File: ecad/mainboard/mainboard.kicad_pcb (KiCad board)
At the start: 4 copper layers, 340 x 220 mm, 124 parts, among them J1 TYPE-C-31-M-12, J2 SWD, J3 UART, SW1 TS-1187A-B-A-B, SW2 TS-1187A-B-A-B, SW3 SW_Push, SW4 SW_Push, U1 NCP1117ST33T3G, U10 DRV5056A3xQDBZxR, U11 DRV5056A3xQDBZxR, U12 DRV5056A3xQDBZxR, U13 DRV5056A3xQDBZxR, U14 DRV5056A3xQDBZxR, U15 DRV5056A3xQDBZxR, U16 DRV5056A3xQDBZxR, U17 DRV5056A3xQDBZxR, U18 DRV5056A3xQDBZxR, U19 DRV5056A3xQDBZxR, U2 USBLC6-2SC6, U20 DRV5056A3xQDBZxR, U21 DRV5056A3xQDBZxR, U22 CD4051BM96, U23 CD4051BM96, U3 W25Q128JVS, U4 74AHCT1G125, U5 RP2040, U6 DRV5056A3xQDBZxR, U7 DRV5056A3xQDBZxR, U8 DRV5056A3xQDBZxR, U9 DRV5056A3xQDBZxR, Y1 ABM8-272-T3

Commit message: WIP: PCB case
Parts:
- C13, C14: value 1u -> 1uF
- D2, D3: value SK6812MINI -> SK6812MINI-EA
- J1: footprint Connector_USB:USB_C_Receptacle_HRO_TYPE-C-31-M-12 -> Udong:USB_C_Receptacle_HRO_TYPE-C-31-M-12
- J2: footprint Connector_JST:JST_SH_BM03B-SRSS-TB_1x03-1MP_P1.00mm_Vertical -> Udong:JST_SH_BM03B-SRSS-TB_1x03-1MP_P1.00mm_Vertical
- moved C32 20.0 mm to (173.5, 136.8)
- moved C36 20.0 mm to (143.6, 131.5)
- moved C37 20.0 mm to (335.6, 147.6)
- moved C38 20.0 mm to (333.4, 136.8)
- moved C11 20.0 mm to (218.7, 65.7)
- moved C18 20.0 mm to (207.0, 77.9)
- moved C19 20.0 mm to (210.2, 77.9)
- moved R13 20.0 mm to (208.7, 76.0)
- moved SW4 20.0 mm to (362.3, 67.2)
- moved R5 20.0 mm to (194.6, 51.6)
- moved C10 20.0 mm to (216.6, 71.9)
- moved C13 20.0 mm to (213.2, 64.0)
- moved C14 20.0 mm to (214.2, 64.0)
- moved C15 20.0 mm to (206.1, 56.6)
- moved C16 20.0 mm to (338.8, 60.5)
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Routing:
- net +1V1: track 15.5 -> 11.8 mm
- net GND: track 153.4 -> 151.8 mm, vias 50 -> 52
- net USB_D+: track 8.52 -> 9.72 mm
- net USB_D-: track 8.57 -> 9.76 mm
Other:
- board text added: "GND"
- board text added: "RX"
- board text added: "SWCLK"
- board text added: "SWD"
- board text added: "TX"

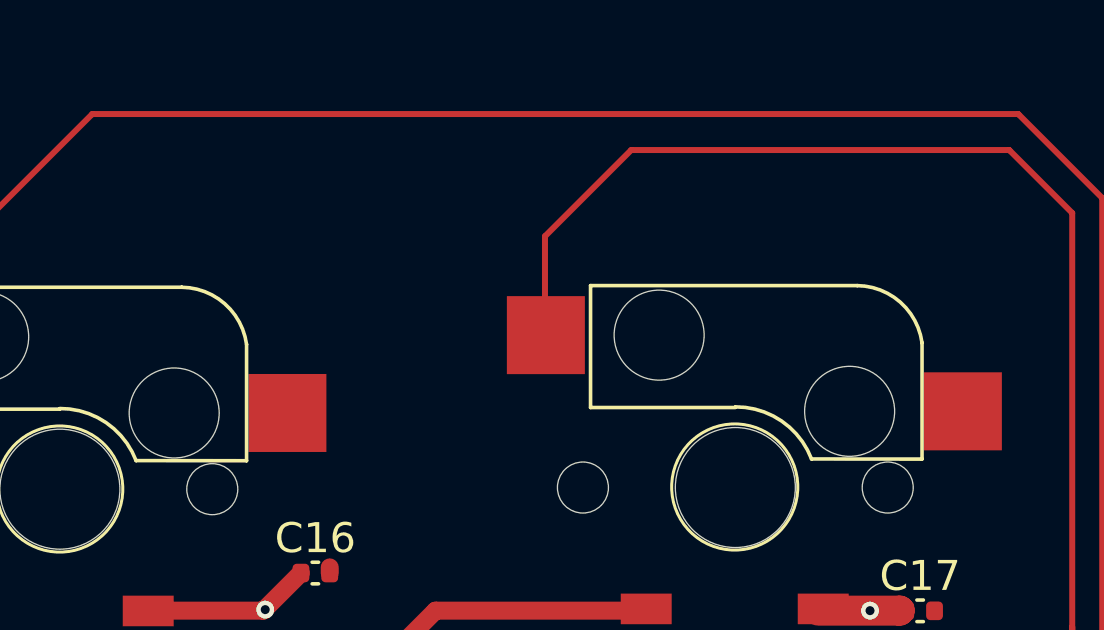
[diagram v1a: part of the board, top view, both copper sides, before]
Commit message: Put labels about button assignment on User.comments layer
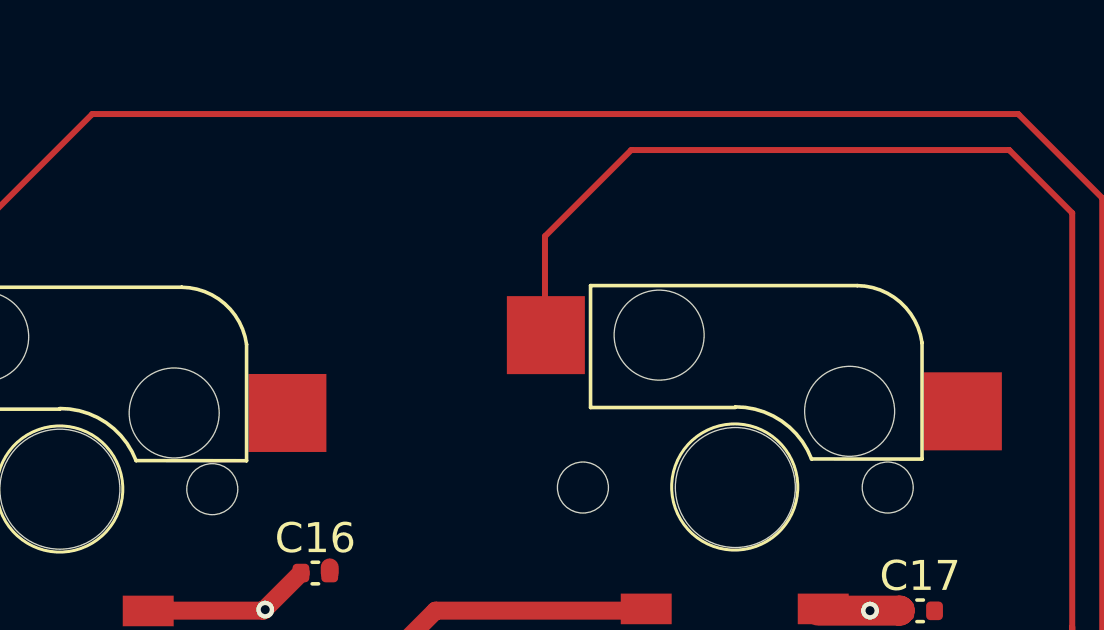
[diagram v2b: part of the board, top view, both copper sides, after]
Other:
- board text added: "M0_0"
- board text added: "M0_1"
- board text added: "M0_2"
- board text added: "M0_3"
- board text added: "M0_4"
- board text added: "M0_5"
- board text added: "M0_6"
- board text added: "M0_7"
- board text added: "M1_10"
- board text added: "M1_11"
- board text added: "M1_12"
- board text added: "M1_13"
- board text added: "M1_14"
- board text added: "M1_15"
- board text added: "M1_8"
- board text added: "M1_9"
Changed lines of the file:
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@@
 		(fp_arc
 			(start 5.436 16.231)
-			(mid 4.002296 15.679932)
+			(mid 4.002293 15.679933)
 			(end 3.277 14.326)
 			(stroke
@@
 		(fp_arc
 			(start 5.436 16.231)
-			(mid 4.002296 15.679932)
+			(mid 4.002293 15.679933)
 			(end 3.277 14.326)
 			(stroke
@@
 		)
 	)
+	(gr_text "M0_4"
+		(at 89 136 0)
+		(layer "Cmts.User")
+		(effects
+			(font
+				(size 3 3)
+				(thickness 0.2)
+			)
+			(justify left bottom)
+		)
+	)
+	(gr_text "M0_5"
+		(at 185 138 0)
+		(layer "Cmts.User")
+		(effects
+			(font
+				(size 3 3)
+				(thickness 0.2)
+			)
+			(justify left bottom)
+		)
+	)
+	(gr_text "M1_9\n"
+		(at 196 158 0)
+		(layer "Cmts.User")
+		(effects
+			(font
+				(size 3 3)
+				(thickness 0.2)
+			)
+			(justify left bottom)
+		)
+	)
+	(gr_text "M0_2"
+		(at 76 102 0)
+		(layer "Cmts.User")
+		(effects
+			(font
+				(size 3 3)
+				(thickness 0.2)
+			)
+			(justify left bottom)
+		)
+	)
+	(gr_text "M0_7"
+		(at 153 131 0)
+		(layer "Cmts.User")
+		(effects
+			(font
+				(size 3 3)
+				(thickness 0.2)
+			)
+			(justify left bottom)
+		)
+	)
+	(gr_text "M1_8"
+		(at 338 130 0)
+		(layer "Cmts.User")
+		(effects
+			(font
+				(size 3 3)
+				(thickness 0.2)
+			)
+			(justify left bottom)
+		)
+	)
+	(gr_text "M1_13\n"
+		(at 312 110 0)
+		(layer "Cmts.User")
+		(effects
+			(font
+				(size 3 3)
+				(thickness 0.2)
+			)
+			(justify left bottom)
+		)
+	)
+	(gr_text "M1_14"
+		(at 257 131 0)
+		(layer "Cmts.User")
+		(effects
+			(font
+				(size 3 3)
+				(thickness 0.2)
+			)
+			(justify left bottom mirror)
+		)
+	)
+	(gr_text "M0_1"
+		(at 116 100 0)
+		(layer "Cmts.User")
+		(effects
+			(font
+				(size 3 3)
+				(thickness 0.2)
+			)
+			(justify left bottom)
+		)
+	)
+	(gr_text "M1_12\n"
+		(at 224 166 0)
+		(layer "Cmts.User")
+		(effects
+			(font
+				(size 3 3)
+				(thickness 0.2)
+			)
+			(justify left bottom)
+		)
+	)
+	(gr_text "M1_15\n"
+		(at 285 98 0)
+		(layer "Cmts.User")
+		(effects
+			(font
+				(size 3 3)
+				(thickness 0.2)
+			)
+			(justify left bottom)
+		)
+	)
+	(gr_text "M0_0"
+		(at 148 95 0)
+		(layer "Cmts.User")
+		(effects
+			(font
+				(size 3 3)
+				(thickness 0.2)
+			)
+			(justify left bottom)
+		)
+	)
+	(gr_text "M1_10"
+		(at 207 111 0)
+		(layer "Cmts.User")
+		(effects
+			(font
+				(size 3 3)
+				(thickness 0.2)
+			)
+			(justify left bottom)
+		)
+	)
+	(gr_text "M1_11\n"
+		(at 292 77 0)
+		(layer "Cmts.User")
+		(effects
+			(font
+				(size 3 3)
+				(thickness 0.2)
+			)
+			(justify left bottom)
+		)
+	)
+	(gr_text "M0_3\n"
+		(at 180 100 0)
+		(layer "Cmts.User")
+		(effects
+			(font
+				(size 3 3)
+				(thickness 0.2)
+			)
+			(justify left bottom)
+		)
+	)
+	(gr_text "M0_6"
+		(at 116 131 0)
+		(layer "Cmts.User")
+		(effects
+			(font
+				(size 3 3)
+				(thickness 0.2)
+			)
+			(justify left bottom)
+		)
+	)

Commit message: Update circuit for the new design
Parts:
- J2: footprint Udong:JST_SH_BM03B-SRSS-TB_1x03-1MP_P1.00mm_Vertical -> Connector_JST:JST_SH_SM03B-SRSS-TB_1x03-1MP_P1.00mm_Horizontal
- moved J2 0.16 mm to (153.6, 43.6), turned to 180 degrees
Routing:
- net SWCLK: track 87.5 -> 88.3 mm
- net SWD: track 92.7 -> 92.1 mm, vias 2 -> 0
- net GND: vias 52 -> 50

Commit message: Update PCB. Next task would be move switch positions
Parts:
- removed C16, C17: 1uF, Capacitor_SMD:C_0402_1005Metric
- removed D2, D3: SK6812MINI-EA, Udong:MX_Socket_LED
- removed J3: UART, Connector_PinSocket_2.54mm:PinSocket_1x03_P2.54mm_Horizontal
- removed R12: 560, Resistor_SMD:R_0402_1005Metric
- removed R4, R6: 20k, Resistor_SMD:R_0402_1005Metric
- removed SW1, SW2: TS-1187A-B-A-B, Button_Switch_SMD:SW_Push_1P1T_XKB_TS-1187A
- removed U4: 74AHCT1G125, Package_TO_SOT_SMD:SOT-353_SC-70-5
- added R30: 10k, Resistor_SMD:R_0402_1005Metric, F.Cu at (203.7, 71.0)
- added R32: 1k, Resistor_SMD:R_0402_1005Metric, F.Cu at (204.1, 69.2)
- added R9: 10k, Resistor_SMD:R_0402_1005Metric, F.Cu at (197.7, 56.7)
- R1: value 220k -> 10k
- R10, R11: footprint Resistor_SMD:R_0402_1005Metric -> Resistor_SMD:R_0603_1608Metric
- moved SW4 267.5 mm to (94.7, 66.2)
- moved SW3 217.4 mm to (122.4, 66.5)
- moved H10 69.5 mm to (175.0, 190.0)
- moved H2 63.2 mm to (70.0, 190.0)
- moved H3 63.2 mm to (350.0, 190.0)
- moved C20 50.0 mm to (85.8, 79.6)
- moved H7 31.6 mm to (255.0, 190.0)
- moved H6 28.5 mm to (256.5, 49.5)
- moved H1 20.0 mm to (70.0, 50.0)
- moved H4 20.0 mm to (350.0, 50.0)
- moved J2 15.5 mm to (169.0, 43.3)
- moved R8 15.0 mm to (221.9, 44.4), turned to 0 degrees
- moved R1 13.5 mm to (217.8, 70.8), turned to 0 degrees
- moved D1 13.5 mm to (219.1, 44.4), turned to 0 degrees
- moved H5 11.3 mm to (146.3, 50.1)
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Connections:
- R1 pad 1: +3.3V -> Net-(U5-GPIO23)
- R1 pad 2: REF_0.6V -> GND
- R5 pad 2: Net-(R5-Pad2) -> BOOTSEL_SW
- SW4 pad 1: DS_1_IN -> BOOTSEL_SW
- U5 pad 2: UART_TX -> GND
- U5 pad 26: RUN -> unconnected-(U5-RUN-Pad26)
- U5 pad 3: UART_RX -> GND
- U5 pad 34: DS_0_IN -> GND
- U5 pad 35: DS_1_IN -> Net-(U5-GPIO23)
- U5 pad 36: LED_OUT -> GND
- U5 pad 4: GND -> DS_0_IN
- U5 pad 5: GND -> DS_1_IN
- U5 pad 6: REF_0.6V -> GND
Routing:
- net BOOTSEL_SW: track 0.00 -> 163.1 mm, vias 0 -> 2
- net LED_OUT_5V: track 94.8 -> 0.00 mm
- net DS_0_IN: track 215.1 -> 126.0 mm, vias 0 -> 2
- net DS_1_IN: track 83.5 -> 2.09 mm
- net RUN: track 58.5 -> 0.00 mm, vias 2 -> 0
- net UART_RX: track 53.0 -> 0.00 mm
- net UART_TX: track 48.1 -> 0.00 mm
- net LED_OUT: track 29.8 -> 0.00 mm
- net GPIO25: track 13.5 -> 34.6 mm
- net Net-(D2-DOUT): track 17.6 -> 0.00 mm
- net GND: track 151.8 -> 135.1 mm, vias 50 -> 42
- net VBUS: track 35.2 -> 22.9 mm, vias 5 -> 2
- net Net-(R5-Pad2): track 11.2 -> 0.00 mm
- net SWD: track 92.1 -> 85.1 mm
- net SWCLK: track 88.3 -> 81.7 mm
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- removed copper zone on In2.Cu, net VBUS
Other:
- board size 340 x 220 mm -> 301.3 x 160 mm
- board text added: "Debug"
- board text removed: "RX"
- board text removed: "TX"

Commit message: Now, Webconf is the root source of switchs coordinates
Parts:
- moved U16 0.10 mm to (205.1, 120.0)
- moved U15 0.08 mm to (190.0, 167.5)
- moved U20 0.08 mm to (250.0, 117.5)
- moved U10 0.08 mm to (85.0, 147.5)
- moved U14 0.08 mm to (335.0, 142.5)
- moved U19 0.08 mm to (310.0, 117.5)
- moved U21 0.08 mm to (280.0, 107.5)
- moved U11 0.06 mm to (175.0, 142.5)
- moved U6 0.06 mm to (145.0, 105.0)
- moved U7 0.06 mm to (115.0, 110.0)
- moved U8 0.06 mm to (85.0, 115.0)
- moved U9 0.06 mm to (175.0, 110.0)
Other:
- board text added: "AS0-0"
- board text added: "AS0-1"
- board text added: "AS0-2"
- board text added: "AS0-3"
- board text added: "AS0-4"
- board text added: "AS0-5"
- board text added: "AS0-6"
- board text added: "AS0-7"
- board text added: "AS1-0"
- board text added: "AS1-1"
- board text added: "AS1-2"
- board text added: "AS1-3"
- board text added: "AS1-4"
- board text added: "AS1-5"
- board text added: "AS1-6"
- board text added: "AS1-7"

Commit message: Make a DigitalSwitch field so that scripts can configure digital-switch related parts easily
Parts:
- K0: renamed from U6; footprint Udong:SW_Cherry_MX_PCB_1.00u_hall_effect -> Udong:SK20_hall_IC
- K1: renamed from U7; footprint Udong:SW_Cherry_MX_PCB_1.00u_hall_effect -> Udong:SK20_hall_IC
- K10: renamed from U16; footprint Udong:SW_Cherry_MX_PCB_1.00u_hall_effect -> Udong:SK20_hall_IC
- K11: renamed from U17; footprint Udong:SW_Cherry_MX_PCB_1.00u_hall_effect -> Udong:SK20_hall_IC
- K12: renamed from U18; footprint Udong:SW_Cherry_MX_PCB_1.00u_hall_effect -> Udong:SK20_hall_IC
- K13: renamed from U19; footprint Udong:SW_Cherry_MX_PCB_1.00u_hall_effect -> Udong:SK20_hall_IC
- K14: renamed from U20; footprint Udong:SW_Cherry_MX_PCB_1.00u_hall_effect -> Udong:SK20_hall_IC
- K15: renamed from U21; footprint Udong:SW_Cherry_MX_PCB_1.00u_hall_effect -> Udong:SK20_hall_IC
- K2: renamed from U8; footprint Udong:SW_Cherry_MX_PCB_1.00u_hall_effect -> Udong:SK20_hall_IC
- K3: renamed from U9; footprint Udong:SW_Cherry_MX_PCB_1.00u_hall_effect -> Udong:SK20_hall_IC
- K4: renamed from U10; footprint Udong:SW_Cherry_MX_PCB_1.00u_hall_effect -> Udong:SK20_hall_IC
- K5: renamed from U11; footprint Udong:SW_Cherry_MX_PCB_1.00u_hall_effect -> Udong:SK20_hall_IC
- K6: renamed from U12; footprint Udong:SW_Cherry_MX_PCB_1.00u_hall_effect -> Udong:SK20_hall_IC
- K7: renamed from U13; footprint Udong:SW_Cherry_MX_PCB_1.00u_hall_effect -> Udong:SK20_hall_IC
- K8: renamed from U14; footprint Udong:SW_Cherry_MX_PCB_1.00u_hall_effect -> Udong:SK20_hall_IC
- K9: renamed from U15; footprint Udong:SW_Cherry_MX_PCB_1.00u_hall_effect -> Udong:SK20_hall_IC
- moved R7 13.9 mm to (216.4, 46.9), turned to 0 degrees
- moved SW3 13.5 mm to (112.9, 57.0)
- moved SW4 13.4 mm to (85.2, 56.7)
- moved C3 12.9 mm to (216.5, 45.9), turned to 0 degrees
- moved R2 11.0 mm to (212.3, 50.1), turned to -90 degrees
- moved R3 7.00 mm to (207.6, 50.5)
- moved C21 1.20 mm to (145.8, 109.4)
- moved D1 1.07 mm to (218.5, 43.5)
- moved R8 1.07 mm to (221.3, 43.5)
- moved C22 0.38 mm to (143.2, 99.4)
- moved R14 0.27 mm to (143.2, 101.0)
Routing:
- net Net-(J1-CC1): track 9.52 -> 2.79 mm
- net GND: track 135.1 -> 130.8 mm, vias 42 -> 40
- net SHIELD: track 35.8 -> 31.9 mm, vias 2 -> 3
- net Net-(J1-CC2): track 6.19 -> 3.38 mm
- net VBUS: track 22.9 -> 25.5 mm
- net GPIO25: track 34.6 -> 36.6 mm
- net +3.3V: track 130.5 -> 129.0 mm
- added copper zone on B.Cu, net SHIELD
